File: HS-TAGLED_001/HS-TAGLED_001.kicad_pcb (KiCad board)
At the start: 2 copper layers, 5 parts, among them J2 Conn_01x03, U1 TSOP59540TR1

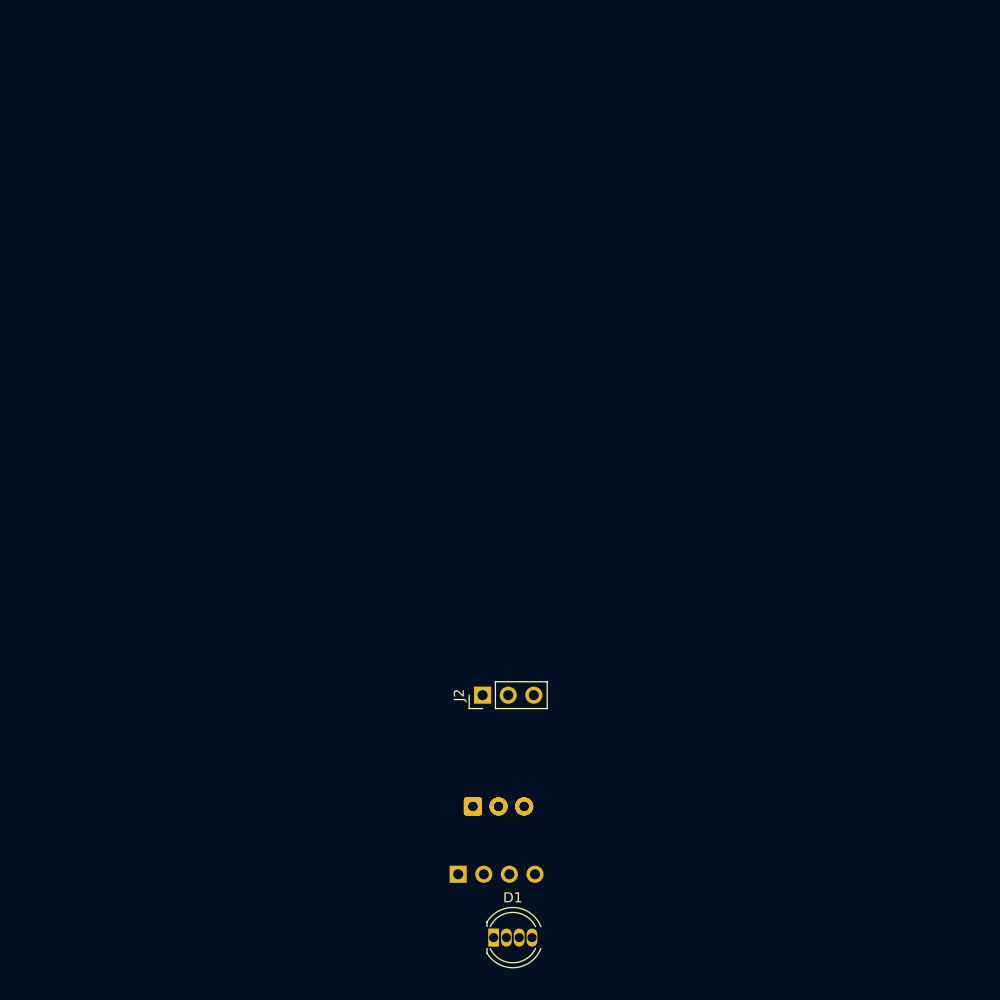
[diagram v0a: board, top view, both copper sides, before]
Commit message: ・HS-TAGLED更新
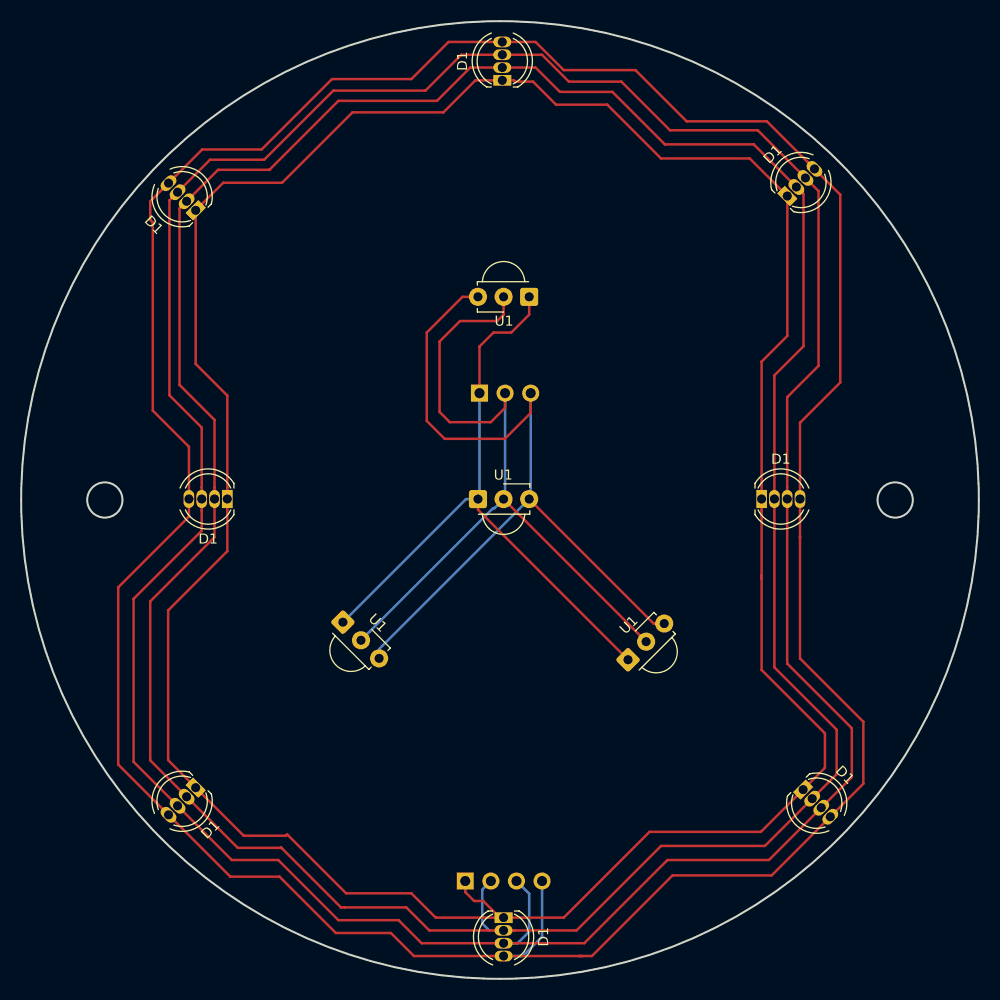
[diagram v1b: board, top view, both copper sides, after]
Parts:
- added D1: LED_ARGB, LED_THT:LED_D5.0mm-4_RGB, F.Cu at (102.6, 90.0)
- added D1: LED_ARGB, LED_THT:LED_D5.0mm-4_RGB, F.Cu at (99.5, 61.4)
- added D1: LED_ARGB, LED_THT:LED_D5.0mm-4_RGB, F.Cu at (99.5, 118.6)
- added D1: LED_ARGB, LED_THT:LED_D5.0mm-4_RGB, F.Cu at (130.0, 131.5)
- added D1: LED_ARGB, LED_THT:LED_D5.0mm-4_RGB, F.Cu at (155.6, 90.0)
- added D1: LED_ARGB, LED_THT:LED_D5.0mm-4_RGB, F.Cu at (158.2, 60.0)
- added D1: LED_ARGB, LED_THT:LED_D5.0mm-4_RGB, F.Cu at (159.7, 118.8)
- added U1: TSOP59540TR1, OptoDevice:Vishay_MINICAST-3Pin, F.Cu at (144.2, 104.2)
- added U1: TSOP59540TR1, OptoDevice:Vishay_MINICAST-3Pin, F.Cu at (130.0, 70.0)
- J2: moved to B.Cu
- U1 (x2): moved to F.Cu
- moved D1 85.0 mm to (129.9, 48.5), turned to 90 degrees
- moved U1 30.6 mm to (130.0, 90.0)
- moved J2 30.0 mm to (127.6, 79.5), turned to 270 degrees
- moved U1 19.9 mm to (115.9, 104.0), turned to 315 degrees
- moved D2 0.97 mm to (126.2, 127.9)
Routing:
- net Net-(D1-Pad4): track 0.00 -> 303.8 mm
- net Net-(D1-Pad3): track 0.00 -> 292.0 mm
- net Net-(D1-Pad2): track 0.00 -> 282.7 mm
- net Net-(D1-Pad1): track 0.00 -> 271.7 mm
- net Net-(J2-Pad3): track 0.00 -> 80.4 mm
- net Net-(J2-Pad2): track 0.00 -> 75.7 mm
- net Net-(J2-Pad1): track 0.00 -> 63.8 mm
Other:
- board outline added: 95 x 95 mm

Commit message: ・各基盤修正
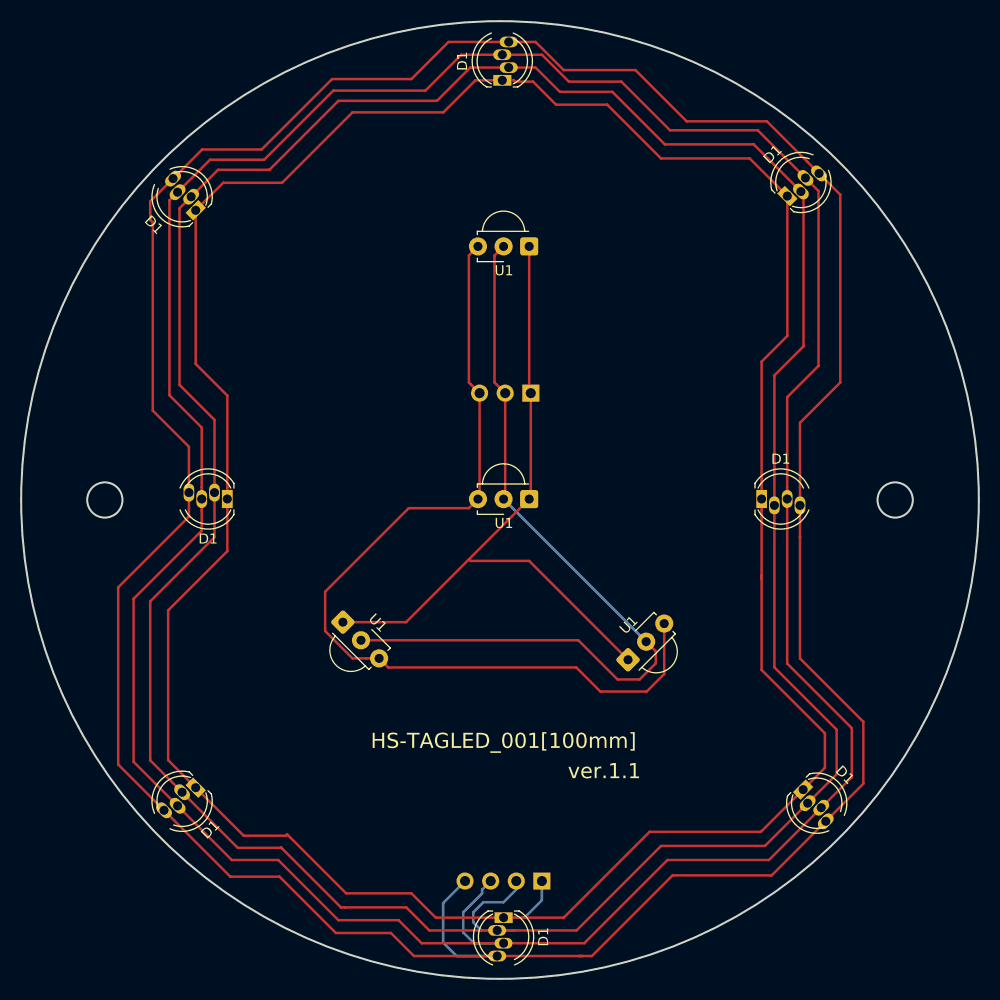
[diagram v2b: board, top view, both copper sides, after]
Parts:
- moved D2 7.60 mm to (133.8, 127.9), turned to 90 degrees
- moved J2 5.09 mm to (132.7, 79.5), turned to 90 degrees
- moved U1 5.00 mm to (130.0, 65.0)
- turned U1 to 180 degrees
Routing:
- net Net-(J2-Pad3): track 80.4 -> 90.7 mm
- net Net-(J2-Pad1): track 63.8 -> 68.6 mm
- net Net-(J2-Pad2): track 75.7 -> 80.0 mm
- net Net-(D1-Pad4): track 303.8 -> 306.6 mm
- net Net-(D1-Pad2): track 282.7 -> 285.5 mm
- net Net-(D1-Pad3): track 292.0 -> 294.1 mm
- net Net-(D1-Pad1): track 271.7 -> 272.5 mm
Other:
- board text added: "HS-TAGLED_001[100mm]"
- board text added: "ver.1.1"

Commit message: ・修正
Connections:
- D1 pad 1: Net-(D1-Pad1) -> Net-(D1-Pad2) (x8)
- D1 pad 2: Net-(D1-Pad2) -> Net-(D1-Pad1) (x8)
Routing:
- net Net-(D1-Pad2): track 285.5 -> 270.4 mm
- net Net-(D1-Pad1): track 272.5 -> 284.1 mm
- net Net-(D1-Pad4): track 306.6 -> 303.8 mm
- net Net-(D1-Pad3): track 294.1 -> 292.3 mm
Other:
- board size 95 x 95 mm -> 81.9 x 3.5 mm

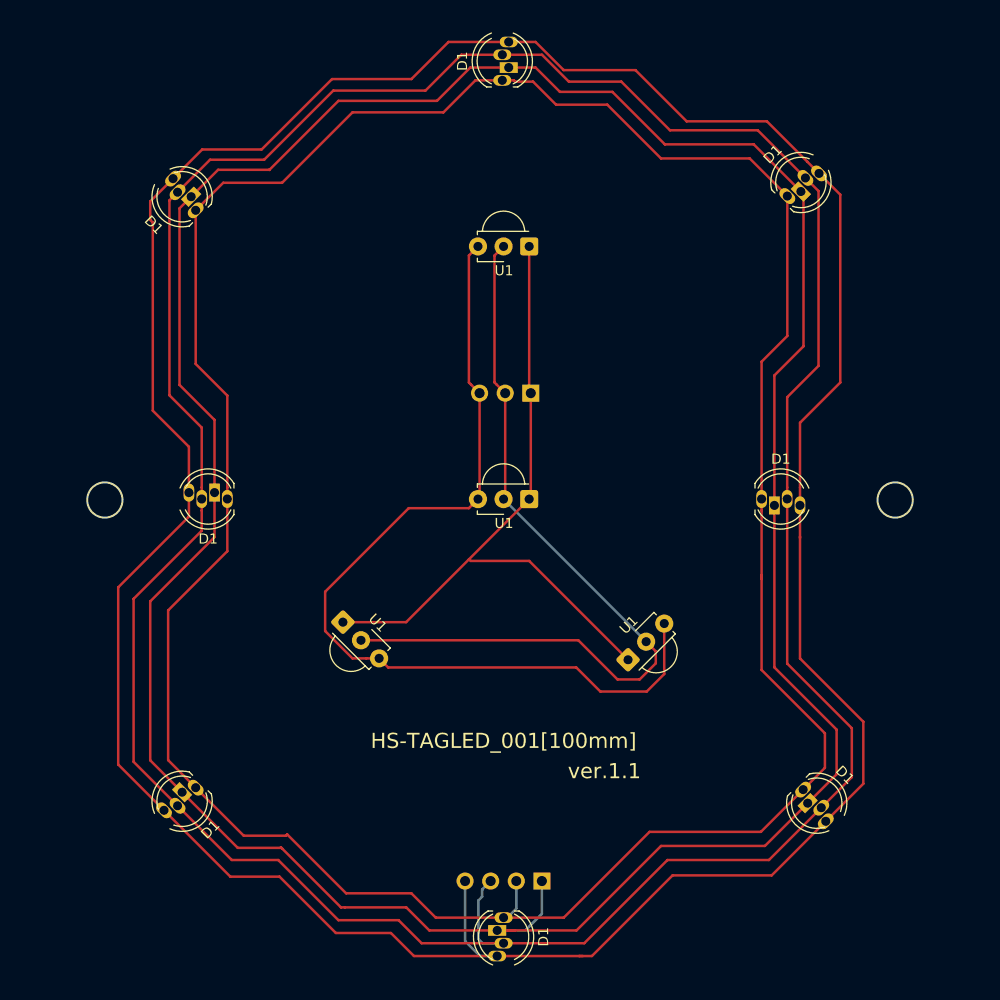
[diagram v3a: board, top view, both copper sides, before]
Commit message: ・不要ファイルの削除
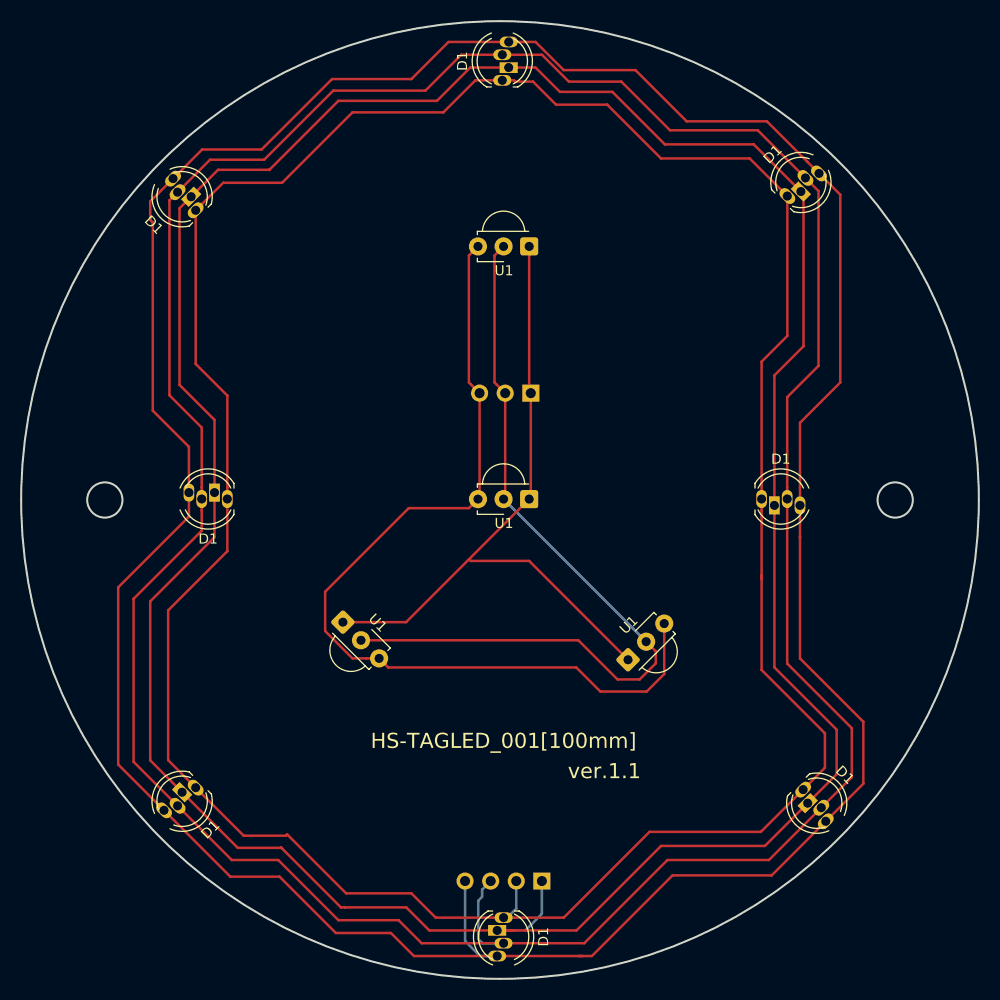
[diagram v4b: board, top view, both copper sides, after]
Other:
- board size 81.9 x 3.5 mm -> 95 x 95 mm
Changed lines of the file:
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@@
-(kicad_pcb (version 20171130) (host pcbnew "(5.1.2-1)-1")
+(kicad_pcb (version 20171130) (host pcbnew "(5.1.2)-2")
   (general
     (thickness 1.6)
@@
     (effects (font (size 1.5 1.5) (thickness 0.3)))
   )
-  (gr_circle (center 129.655143 90.11) (end 177.155142 90.11) (layer Eco2.User) (width 0.2))
+  (gr_circle (center 129.655143 90.11) (end 177.155142 90.11) (layer Edge.Cuts) (width 0.2))
   (gr_circle (center 90.4558 90.1089) (end 92.205801 90.1089) (layer Edge.Cuts) (width 0.2))
   (gr_circle (center 168.8558 90.1089) (end 170.605799 90.1089) (layer Edge.Cuts) (width 0.2))
-  (segment (start 104.230352 123.411) (end 99.467176 118.647824) (width 0.25) (layer F.Cu) (net 2))
-  (segment (start 108.42 123.411) (end 104.230352 123.411) (width 0.25) (layer F.Cu) (net 2))
-  (segment (start 108.547 123.284) (end 108.42 123.411) (width 0.25) (layer F.Cu) (net 2))
-  (segment (start 114.389 129.126) (end 108.547 123.284) (width 0.25) (layer F.Cu) (net 2))
-  (segment (start 120.866 129.126) (end 114.389 129.126) (width 0.25) (layer F.Cu) (net 2))
-  (segment (start 123.279 131.539) (end 120.866 129.126) (width 0.25) (layer F.Cu) (net 2))
-  (segment (start 130.01 131.539) (end 123.279 131.539) (width 0.25) (layer F.Cu) (net 2))
-  (segment (start 102.605 95.19) (end 102.605 90.01) (width 0.25) (layer F.Cu) (net 2))
-  (segment (start 96.736 101.059) (end 102.605 95.19) (width 0.25) (layer F.Cu) (net 2))
-  (segment (start 96.736 115.916648) (end 96.736 101.059) (width 0.25) (layer F.Cu) (net 2))
-  (segment (start 99.467176 118.647824) (end 96.736 115.916648) (width 0.25) (layer F.Cu) (net 2))
-  (segment (start 155.605 91.16) (end 155.605 90.01) (width 0.25) (layer F.Cu) (net 2))
-  (segment (start 158.157038 59.957962) (end 158.157038 73.834038) (width 0.25) (layer F.Cu) (net 2))
-  (segment (start 155.605 76.386076) (end 155.605 90.01) (width 0.25) (layer F.Cu) (net 2))
-  (segment (start 158.157038 73.834038) (end 155.605 76.386076) (width 0.25) (layer F.Cu) (net 2))
-  (segment (start 99.467176 61.372176) (end 99.467176 76.612176) (width 0.25) (layer F.Cu) (net 2))
-  (segment (start 102.605 88.86) (end 102.605 90.01) (width 0.25) (layer F.Cu) (net 2))
-  (segment (start 102.605 79.75) (end 102.605 88.86) (width 0.25) (layer F.Cu) (net 2))
-  (segment (start 99.467176 76.612176) (end 102.605 79.75) (width 0.25) (layer F.Cu) (net 2))
-  (segment (start 102.198352 58.641) (end 99.467176 61.372176) (width 0.25) (layer F.Cu) (net 2))
-  (segment (start 129.883 48.481) (end 127.216 48.481) (width 0.25) (layer F.Cu) (net 2))
-  (segment (start 108.039 58.641) (end 102.198352 58.641) (width 0.25) (layer F.Cu) (net 2))
-  (segment (start 115.024 51.656) (end 108.039 58.641) (width 0.25) (layer F.Cu) (net 2))
-  (segment (start 124.041 51.656) (end 115.024 51.656) (width 0.25) (layer F.Cu) (net 2))
-  (segment (start 127.216 48.481) (end 124.041 51.656) (width 0.25) (layer F.Cu) (net 2))
-  (segment (start 131.033 48.481) (end 131.16 48.608) (width 0.25) (layer F.Cu) (net 2))
-  (segment (start 129.883 48.481) (end 131.033 48.481) (width 0.25) (layer F.Cu) (net 2))
-  (segment (start 131.16 48.608) (end 132.931 48.608) (width 0.25) (layer F.Cu) (net 2))
-  (segment (start 132.931 48.608) (end 135.217 50.894) (width 0.25) (layer F.Cu) (net 2))
-  (segment (start 135.217 50.894) (end 140.297 50.894) (width 0.25) (layer F.Cu) (net 2))
-  (segment (start 140.297 50.894) (end 145.631 56.228) (width 0.25) (layer F.Cu) (net 2))
-  (segment (start 154.427076 56.228) (end 158.157038 59.957962) (width 0.25) (layer F.Cu) (net 2))
-  (segment (start 145.631 56.228) (end 154.427076 56.228) (width 0.25) (layer F.Cu) (net 2))
-  (segment (start 129.645 131.539) (end 130.01 131.539) (width 0.25) (layer F.Cu) (net 2))
-  (segment (start 130.01 131.539) (end 135.979 131.539) (width 0.25) (layer F.Cu) (net 2))
-  (segment (start 135.979 131.539) (end 144.488 123.03) (width 0.25) (layer F.Cu) (net 2))
-  (segment (start 155.537 123.03) (end 159.728 118.839) (width 0.25) (layer F.Cu) (net 2))
-  (segment (start 144.488 123.03) (end 155.537 123.03) (width 0.25) (layer F.Cu) (net 2))
-  (segment (start 155.605 97.952) (end 155.605 97.562) (width 0.25) (layer F.Cu) (net 2))
-  (segment (start 155.605 97.562) (end 155.605 91.16) (width 0.25) (layer F.Cu) (net 2))
-  (segment (start 161.887 113.251) (end 161.887 116.68) (width 0.25) (layer F.Cu) (net 2))
-  (segment (start 161.887 116.68) (end 159.728 118.839) (width 0.25) (layer F.Cu) (net 2))
-  (segment (start 155.605 106.969) (end 161.887 113.251) (width 0.25) (layer F.Cu) (net 2))
-  (segment (start 155.605 97.562) (end 155.605 106.969) (width 0.25) (layer F.Cu) (net 2))
   (segment (start 131.16 132.809) (end 130.01 132.809) (width 0.25) (layer F.Cu) (net 1))
   (segment (start 130.01 132.809) (end 122.644 132.809) (width 0.25) (layer F.Cu) (net 1))
@@
   (segment (start 132.169 132.809) (end 133.81 131.168) (width 0.25) (layer B.Cu) (net 1))
   (segment (start 129.375 132.809) (end 132.169 132.809) (width 0.25) (layer B.Cu) (net 1))
+  (segment (start 104.230352 123.411) (end 99.467176 118.647824) (width 0.25) (layer F.Cu) (net 2))
+  (segment (start 108.42 123.411) (end 104.230352 123.411) (width 0.25) (layer F.Cu) (net 2))
+  (segment (start 108.547 123.284) (end 108.42 123.411) (width 0.25) (layer F.Cu) (net 2))
+  (segment (start 114.389 129.126) (end 108.547 123.284) (width 0.25) (layer F.Cu) (net 2))
+  (segment (start 120.866 129.126) (end 114.389 129.126) (width 0.25) (layer F.Cu) (net 2))
+  (segment (start 123.279 131.539) (end 120.866 129.126) (width 0.25) (layer F.Cu) (net 2))
+  (segment (start 130.01 131.539) (end 123.279 131.539) (width 0.25) (layer F.Cu) (net 2))
+  (segment (start 102.605 95.19) (end 102.605 90.01) (width 0.25) (layer F.Cu) (net 2))
+  (segment (start 96.736 101.059) (end 102.605 95.19) (width 0.25) (layer F.Cu) (net 2))
+  (segment (start 96.736 115.916648) (end 96.736 101.059) (width 0.25) (layer F.Cu) (net 2))
+  (segment (start 99.467176 118.647824) (end 96.736 115.916648) (width 0.25) (layer F.Cu) (net 2))
+  (segment (start 155.605 91.16) (end 155.605 90.01) (width 0.25) (layer F.Cu) (net 2))
+  (segment (start 158.157038 59.957962) (end 158.157038 73.834038) (width 0.25) (layer F.Cu) (net 2))
+  (segment (start 155.605 76.386076) (end 155.605 90.01) (width 0.25) (layer F.Cu) (net 2))
+  (segment (start 158.157038 73.834038) (end 155.605 76.386076) (width 0.25) (layer F.Cu) (net 2))
+  (segment (start 99.467176 61.372176) (end 99.467176 76.612176) (width 0.25) (layer F.Cu) (net 2))
+  (segment (start 102.605 88.86) (end 102.605 90.01) (width 0.25) (layer F.Cu) (net 2))
+  (segment (start 102.605 79.75) (end 102.605 88.86) (width 0.25) (layer F.Cu) (net 2))
+  (segment (start 99.467176 76.612176) (end 102.605 79.75) (width 0.25) (layer F.Cu) (net 2))
+  (segment (start 102.198352 58.641) (end 99.467176 61.372176) (width 0.25) (layer F.Cu) (net 2))
+  (segment (start 129.883 48.481) (end 127.216 48.481) (width 0.25) (layer F.Cu) (net 2))
+  (segment (start 108.039 58.641) (end 102.198352 58.641) (width 0.25) (layer F.Cu) (net 2))
+  (segment (start 115.024 51.656) (end 108.039 58.641) (width 0.25) (layer F.Cu) (net 2))
+  (segment (start 124.041 51.656) (end 115.024 51.656) (width 0.25) (layer F.Cu) (net 2))
+  (segment (start 127.216 48.481) (end 124.041 51.656) (width 0.25) (layer F.Cu) (net 2))
+  (segment (start 131.033 48.481) (end 131.16 48.608) (width 0.25) (layer F.Cu) (net 2))
+  (segment (start 129.883 48.481) (end 131.033 48.481) (width 0.25) (layer F.Cu) (net 2))
+  (segment (start 131.16 48.608) (end 132.931 48.608) (width 0.25) (layer F.Cu) (net 2))
+  (segment (start 132.931 48.608) (end 135.217 50.894) (width 0.25) (layer F.Cu) (net 2))
+  (segment (start 135.217 50.894) (end 140.297 50.894) (width 0.25) (layer F.Cu) (net 2))
+  (segment (start 140.297 50.894) (end 145.631 56.228) (width 0.25) (layer F.Cu) (net 2))
+  (segment (start 154.427076 56.228) (end 158.157038 59.957962) (width 0.25) (layer F.Cu) (net 2))
+  (segment (start 145.631 56.228) (end 154.427076 56.228) (width 0.25) (layer F.Cu) (net 2))
+  (segment (start 129.645 131.539) (end 130.01 131.539) (width 0.25) (layer F.Cu) (net 2))
+  (segment (start 130.01 131.539) (end 135.979 131.539) (width 0.25) (layer F.Cu) (net 2))
+  (segment (start 135.979 131.539) (end 144.488 123.03) (width 0.25) (layer F.Cu) (net 2))
+  (segment (start 155.537 123.03) (end 159.728 118.839) (width 0.25) (layer F.Cu) (net 2))
+  (segment (start 144.488 123.03) (end 155.537 123.03) (width 0.25) (layer F.Cu) (net 2))
+  (segment (start 155.605 97.952) (end 155.605 97.562) (width 0.25) (layer F.Cu) (net 2))
+  (segment (start 155.605 97.562) (end 155.605 91.16) (width 0.25) (layer F.Cu) (net 2))
+  (segment (start 161.887 113.251) (end 161.887 116.68) (width 0.25) (layer F.Cu) (net 2))
+  (segment (start 161.887 116.68) (end 159.728 118.839) (width 0.25) (layer F.Cu) (net 2))
+  (segment (start 155.605 106.969) (end 161.887 113.251) (width 0.25) (layer F.Cu) (net 2))
+  (segment (start 155.605 97.562) (end 155.605 106.969) (width 0.25) (layer F.Cu) (net 2))
   (segment (start 130.375 131.539) (end 130.01 131.539) (width 0.25) (layer B.Cu) (net 2))
   (segment (start 131.27 130.644) (end 130.375 131.539) (width 0.25) (layer B.Cu) (net 2))
